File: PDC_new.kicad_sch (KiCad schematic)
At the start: 83 parts, among them J1 Conn_01x02_Pin, J10 Conn_01x02_Pin, J11 XT90PW(2+2)-M.G.Y, J12 Conn_01x02_Pin, J13 Conn_01x02_Pin, J14 Conn_01x02_Pin, J15 Conn_01x02_Pin, J2 Conn_01x02_Pin, J3 Conn_01x02_Pin, J4 Conn_01x02_Pin, J5 Conn_01x02_Pin, J6 Conn_01x02_Pin, J7 Conn_01x02_Pin, J8 Conn_01x02_Pin, J9 Conn_01x02_Pin, Q2 IRF540NSTRLPBF, U1 TPSI3050QDWZRQ1, U10 LM393LVDR, U11 IPB017N10N5ATMA1, U12 IPB017N10N5ATMA1, U14 IPB017N10N5ATMA1, U2 TPSI3050QDWZRQ1, U4 74HC74, U5 URB4805LD-60WR3, U6 IPB017N10N5ATMA1, U7 TLC555CDR, U8 SN74HC08D, U9 SN74HC14DR

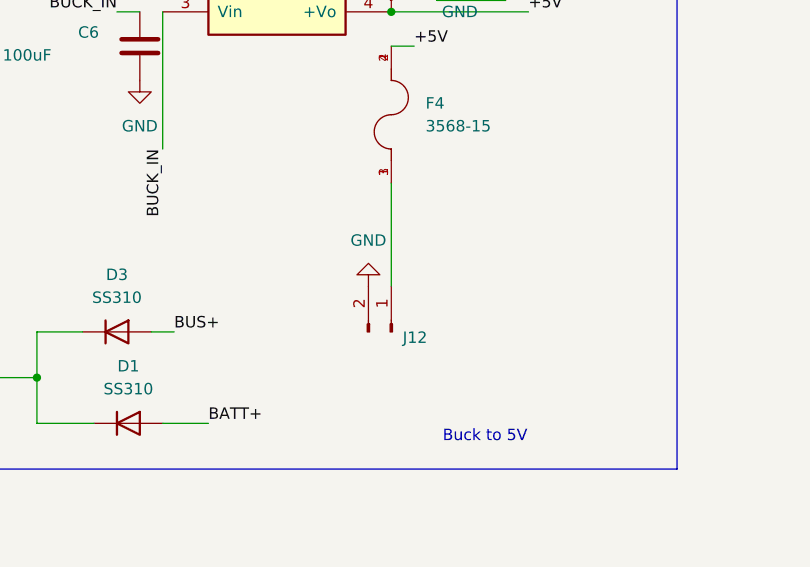
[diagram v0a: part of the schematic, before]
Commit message: Final touchup, solved vias issues and XT30 connector mismatch
Co-Authored-By: Claude Opus 5.5 <noreply@anthropic.com>
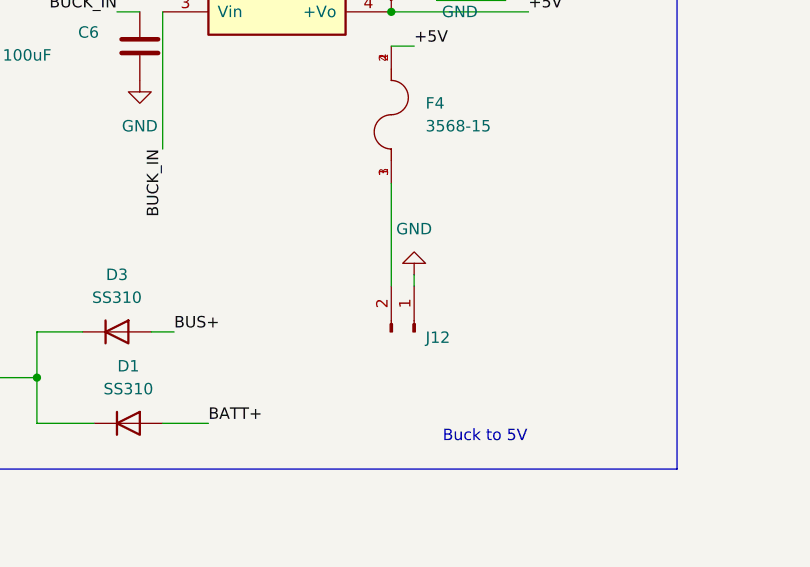
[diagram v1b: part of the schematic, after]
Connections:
- net GND: now also J12.1 (Pin_1); no longer J12.2 (Pin_2)
- net at F4.1, F4.3: now also J12.2 (Pin_2); no longer J12.1 (Pin_1)
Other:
- moved on the sheet: J12
